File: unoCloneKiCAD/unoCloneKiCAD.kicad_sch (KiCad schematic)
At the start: 8 parts, among them U1 ATmega328P-A, Y1 16MHz, C13738

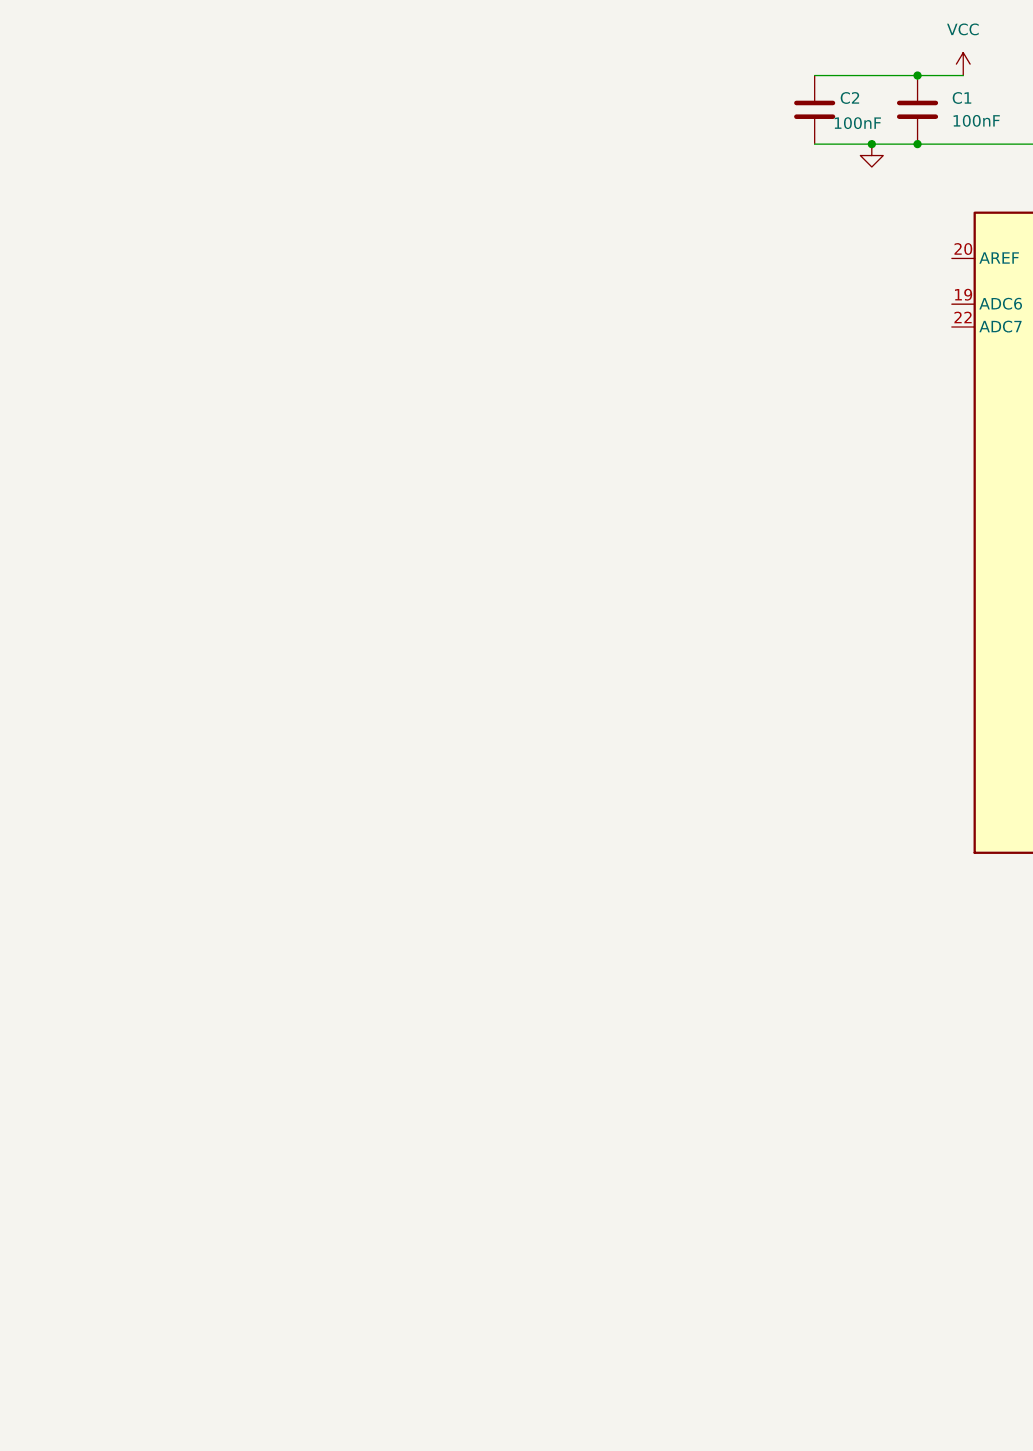
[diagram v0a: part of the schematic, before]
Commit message: Changed to P-PU
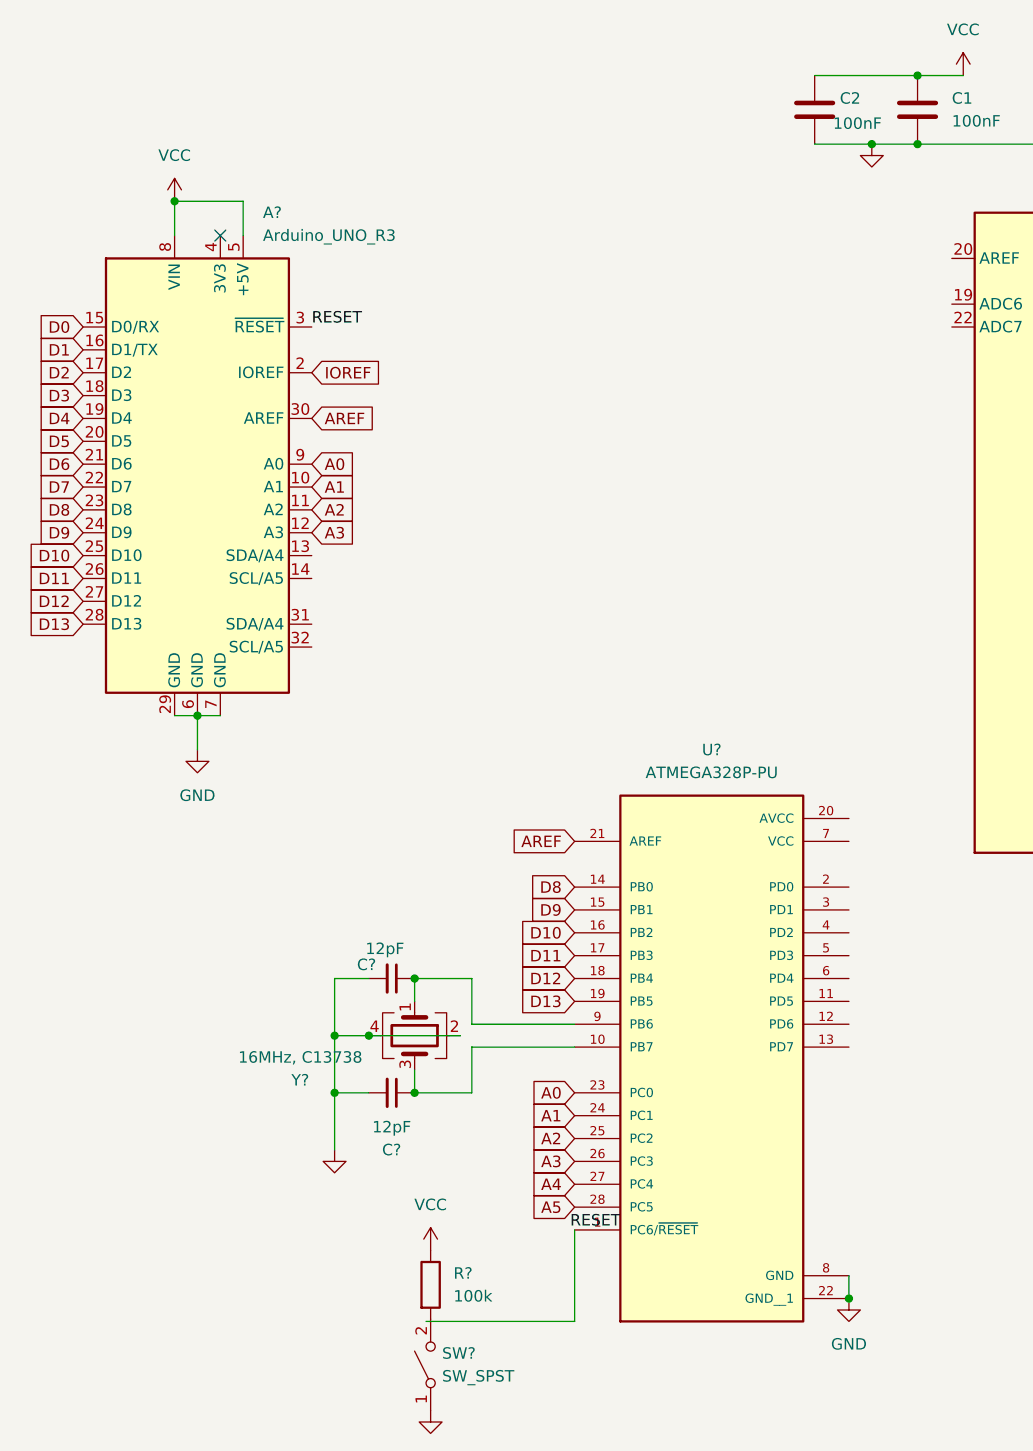
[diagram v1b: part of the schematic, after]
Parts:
- added A?: Arduino_UNO_R3, Module:Arduino_UNO_R3, symbol MCU_Module:Arduino_UNO_R3
- added C? (x2): 12pF, symbol Device:C_Small
- added R?: 100k, symbol Device:R
- added SW?: SW_SPST, symbol Switch:SW_SPST
- added U?: ATMEGA328P-PU, ATMEGA328P-PU:DIP794W46P254L2967H457Q28B, symbol ATMEGA328P-PU:ATMEGA328P-PU
- added Y?: 16MHz, C13738, symbol Device:Crystal_GND24
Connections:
- net GND: now also A?.29 (GND), A?.6 (GND), A?.7 (GND), C?.2, C?.2, SW?.1 (A), U?.22 (GND__1), U?.8 (GND), Y?.2, Y?.4
- net RESET: now also A?.3 (~{RESET})
- net VCC: now also A?.5 (+5V), A?.8 (VIN), R?.1
- new net: R?.2, SW?.2 (B)
- new net: C?.1, U?.9 (PB6), Y?.1
- new net: C?.1, U?.10 (PB7), Y?.3
- new net A0: A?.9 (A0), U?.23 (PC0)
- new net A1: A?.10 (A1), U?.24 (PC1)
- new net A2: A?.11 (A2), U?.25 (PC2)
- new net A3: A?.12 (A3), U?.26 (PC3)
- new net A4: U?.27 (PC4)
- new net A5: U?.28 (PC5)
- new net AREF: A?.30 (AREF), U?.21 (AREF)
- new net D0: A?.15 (D0/RX)
- new net D1: A?.16 (D1/TX)
- new net D10: A?.25 (D10), U?.16 (PB2)
- new net D11: A?.26 (D11), U?.17 (PB3)
- new net D12: A?.27 (D12), U?.18 (PB4)
- new net D13: A?.28 (D13), U?.19 (PB5)
- new net D2: A?.17 (D2)
- new net D3: A?.18 (D3)
- new net D4: A?.19 (D4)
- new net D5: A?.20 (D5)
- new net D6: A?.21 (D6)
- new net D7: A?.22 (D7)
- new net D8: A?.23 (D8), U?.14 (PB0)
- new net D9: A?.24 (D9), U?.15 (PB1)
- new net IOREF: A?.2 (IOREF)
- no-connect marks 0 -> 1

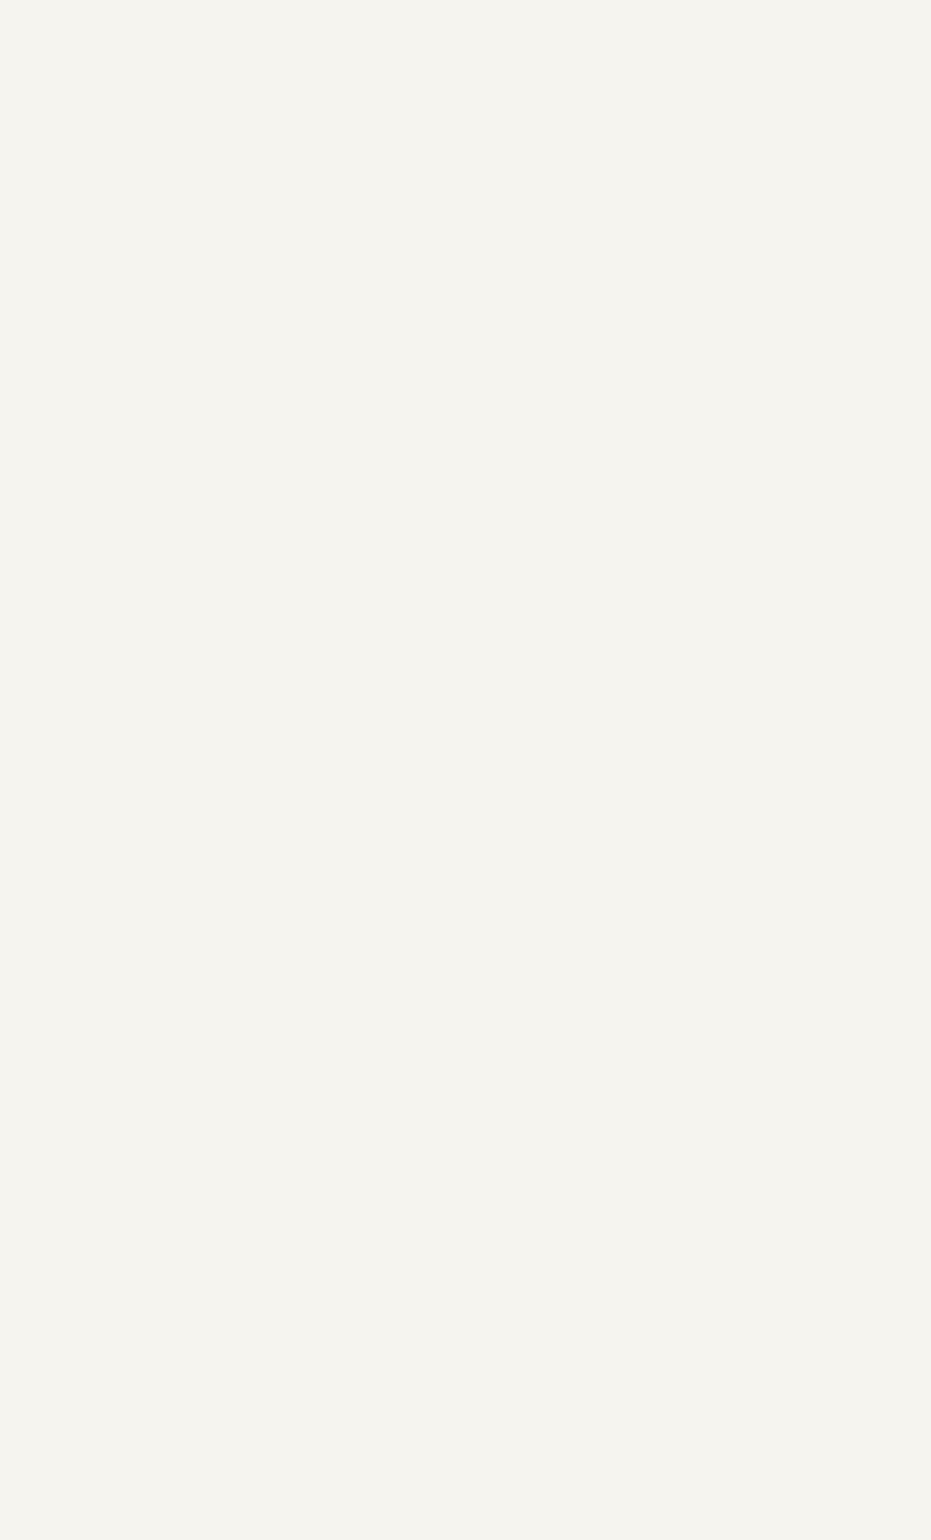
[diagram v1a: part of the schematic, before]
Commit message: USB circuits start
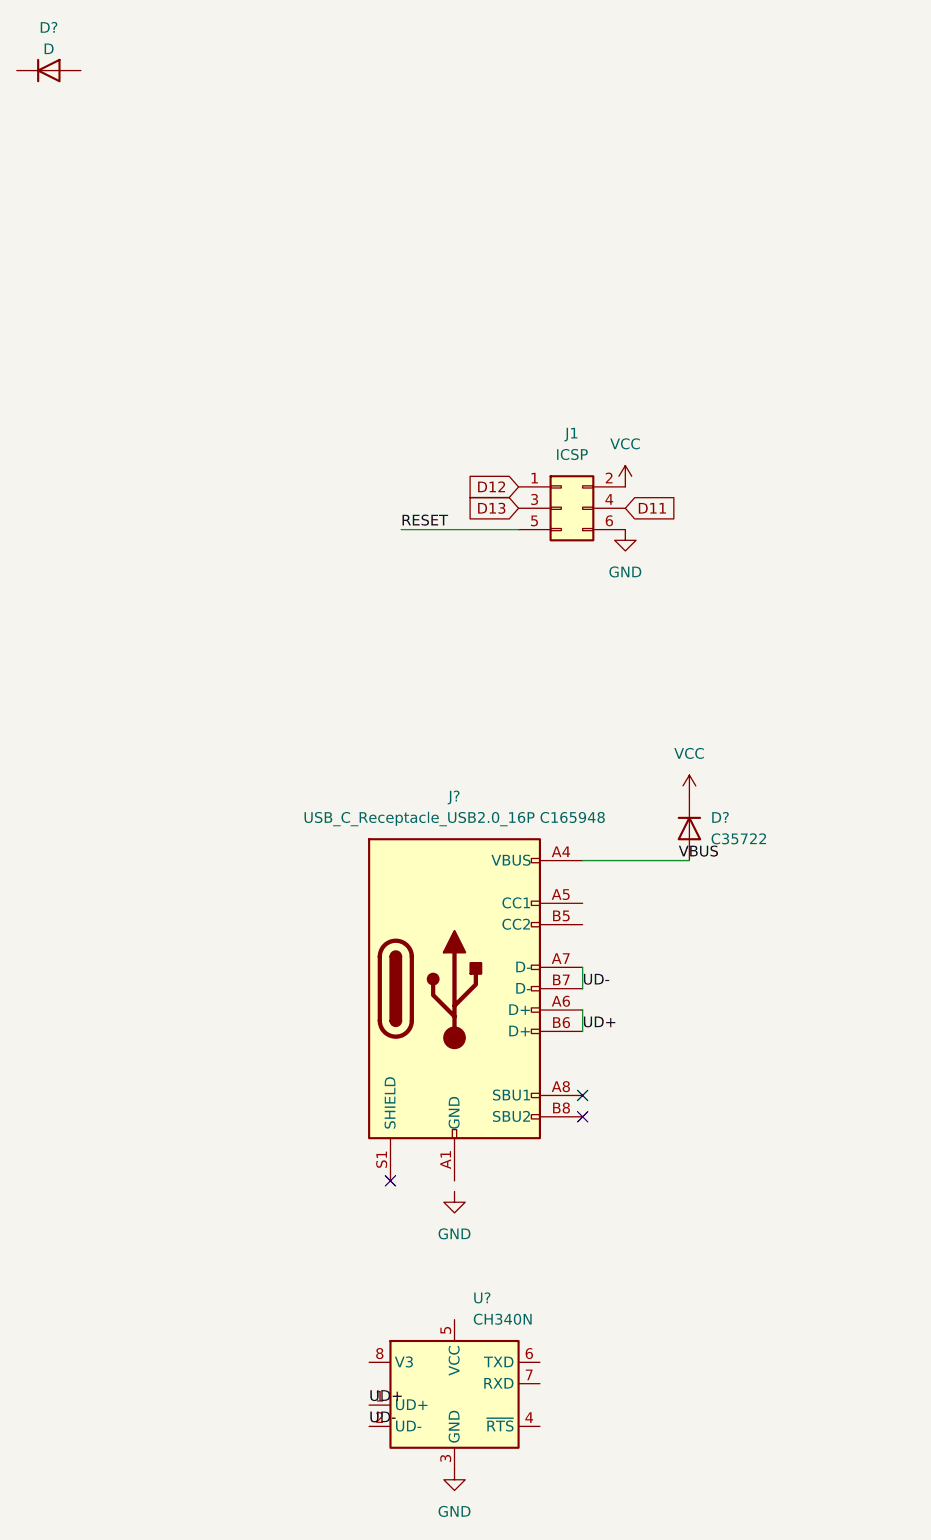
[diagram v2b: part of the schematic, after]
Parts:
- added D?: D, symbol Device:D
- added D?: C35722, symbol Device:D
- added J1: ICSP, symbol Connector_Generic:Conn_02x03_Odd_Even
- added J?: USB_C_Receptacle_USB2.0_16P C165948, symbol Connector:USB_C_Receptacle_USB2.0_16P
- added U?: CH340N, Package_SO:SOP-8_3.9x4.9mm_P1.27mm, symbol Interface_USB:CH340N
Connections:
- net D11: now also J1.4 (Pin_4)
- net D12: now also J1.1 (Pin_1)
- net D13: now also J1.3 (Pin_3)
- net GND: now also J1.6 (Pin_6), U?.3 (GND)
- net RESET: now also J1.5 (Pin_5)
- net VCC: now also D?.1 (K), J1.2 (Pin_2)
- new net: J?.A1 (GND), J?.A12 (GND), J?.B1 (GND), J?.B12 (GND)
- new net UD+: J?.A6 (D+), J?.B6 (D+), U?.1 (UD+)
- new net UD-: J?.A7 (D-), J?.B7 (D-), U?.2 (UD-)
- new net VBUS: D?.2 (A), J?.A4 (VBUS), J?.A9 (VBUS), J?.B4 (VBUS), J?.B9 (VBUS)
- no-connect marks 1 -> 4
